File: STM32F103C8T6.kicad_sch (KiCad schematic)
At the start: 28 parts, among them J4 Conn_02x03_Odd_Even, J5 Conn_01x05_Male, J6 Conn_01x04_Male, SW1 PTS810, U3 MCU_STM32F103C8Tx, Y1 16MHz

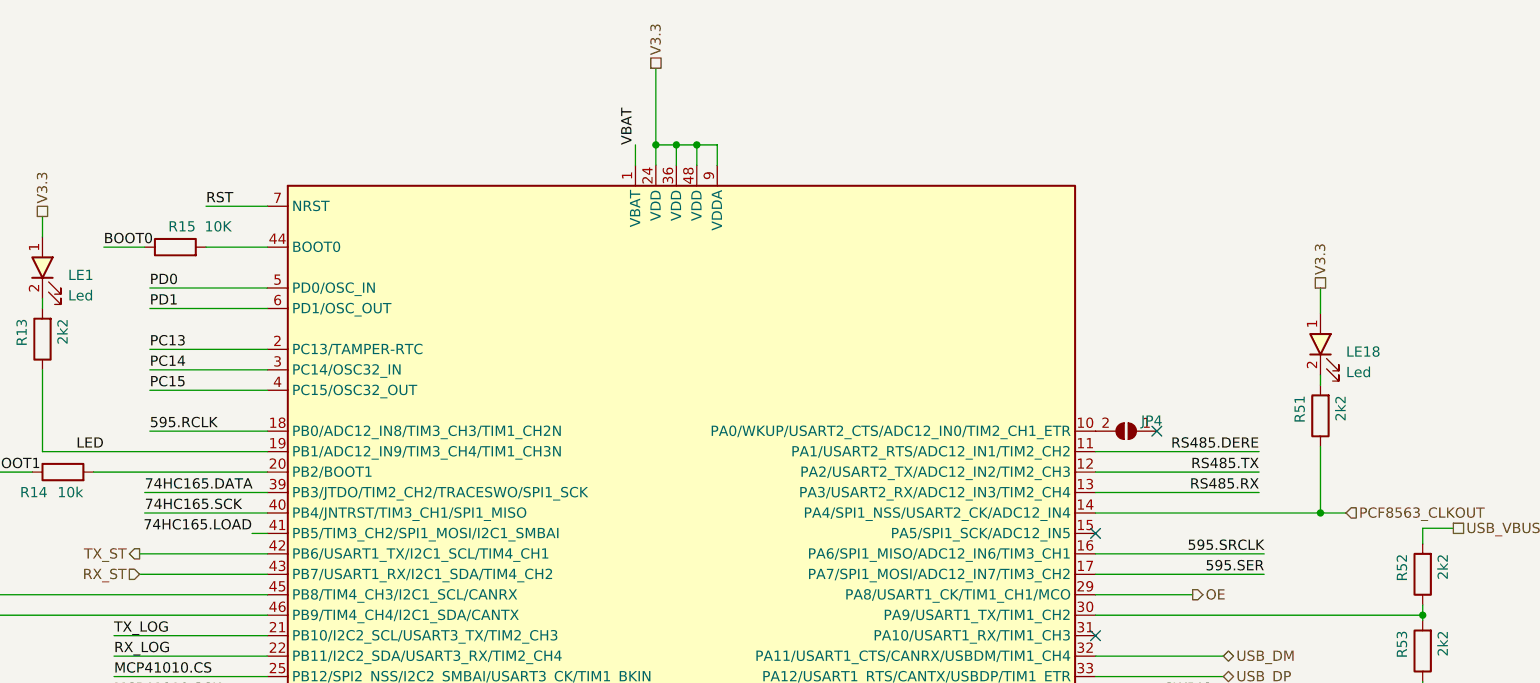
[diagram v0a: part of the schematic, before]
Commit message: finish some unconnect pins, draw edge cut board
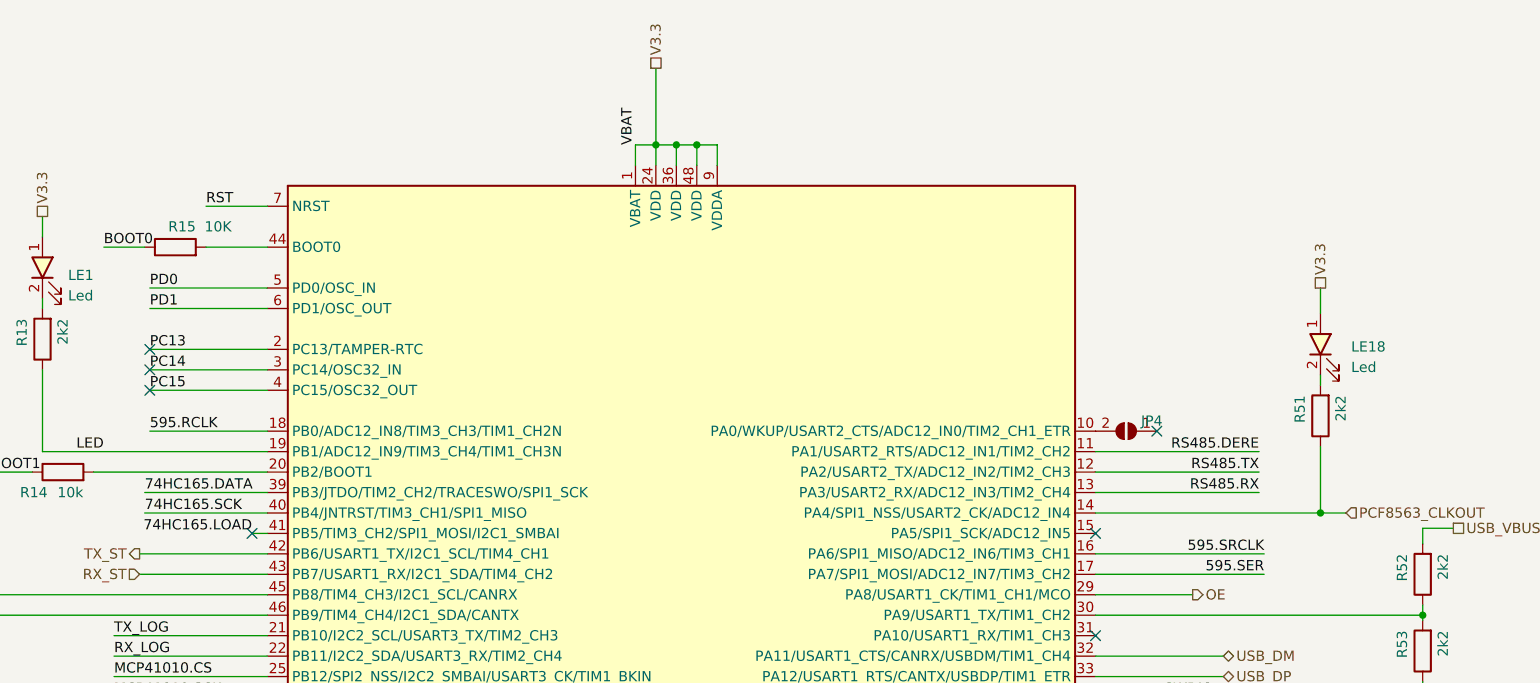
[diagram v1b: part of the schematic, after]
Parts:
- removed LE18: Led, SpiritBoi_Footprint_Library:LED_0603, symbol IVS_SYMBOLS:Led
- added LE18: Led, SpiritBoi_Footprint_Library:LED_0603, symbol SpiritBoi_Library:Led
- JP4: now left out of the parts list
- R14: symbol Thu_vien_kicad:R -> SpiritBoi_Library:R
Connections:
- net VBAT is gone; now on net V3.3: U3.1 (VBAT)
- net V3.3: now also LE18.1
- net at R51.2: now also LE18.2
- no-connect marks 5 -> 9
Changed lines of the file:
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@@
 	)
 	(no_connect
+		(at 156.845 147.32)
+	)
+	(no_connect
+		(at 169.545 170.18)
+	)
+	(no_connect
+		(at 156.845 152.4)
+	)
+	(no_connect
 		(at 274.32 182.88)
 	)
@@
 	)
 	(no_connect
+		(at 156.845 149.86)
+	)
+	(no_connect
 		(at 274.32 170.18)
 	)
@@
 	(wire
 		(pts
+			(xy 217.17 121.92) (xy 219.71 121.92)
+		)
+		(stroke
+			(width 0)
+			(type default)
+		)
+	)
+	(wire
+		(pts
 			(xy 111.76 52.705) (xy 111.76 60.96)
 		)
@@
 		(unit 1)
 		(exclude_from_sim no)
-		(in_bom yes)
+		(in_bom no)
 		(on_board yes)
 		(dnp no)
@@
 	)
 	(symbol
+		(lib_id "SpiritBoi_Library:Led")
+		(at 302.26 147.955 90)
+		(unit 1)
+		(exclude_from_sim no)
+		(in_bom yes)
+		(on_board yes)
+		(dnp no)
+		(fields_autoplaced yes)
+		(property "Reference" "LE18"
+			(at 306.07 147.0024 90)
+			(effects
+				(font
+					(size 1.27 1.27)
+				)
+				(justify right)
+			)
+		)
+		(property "Value" "Led"
+			(at 306.07 149.5424 90)
+			(effects
+				(font
+					(size 1.27 1.27)
+				)
+				(justify right)
+			)
+		)
+		(property "Footprint" "SpiritBoi_Footprint_Library:LED_0603"
+			(at 302.514 147.193 0)
+			(effects
+				(font
+					(size 1.27 1.27)
+				)
+				(hide yes)
+			)
+		)
+		(property "Datasheet" ""
+			(at 302.514 147.193 0)
+			(effects
+				(font
+					(size 1.27 1.27)
+				)
+				(hide yes)
+			)
+		)
+		(property "Description" ""
+			(at 302.26 147.955 0)
+			(effects
+				(font
+					(size 1.27 1.27)
+				)
+				(hide yes)
+			)
+		)
+		(pin "2"
+		)
+		(pin "1"
+		)
+		(instances
+			(project "DongTamV2"
+				(path "/2303d546-b88a-4ab0-aee1-26e3b32ac9d7/de1d919d-cc07-489f-afed-971dd930ed54"
+					(reference "LE18")
+					(unit 1)
+				)
+			)
+		)
+	)
+	(symbol
 		(lib_id "SpiritBoi_Library:MCU_STM32F103C8Tx")
 		(at 222.25 165.1 0)
@@
 			)
 		)
-		(property "Description" ""
+		(property "Description" "Resistor"
 			(at 106.68 170.18 0)
 			(effects
@@
 	)
 	(symbol
-		(lib_id "Thu_vien_kicad:R")
+		(lib_id "SpiritBoi_Library:R")
 		(at 146.05 162.56 90)
 		(unit 1)
@@
 			)
 		)
-		(property "Description" ""
+		(property "Description" "Resistor"
 			(at 146.05 162.56 0)
 			(effects
@@
 					(unit 1)
 				)
-			)
-		)
-	)
-	(symbol
-		(lib_id "IVS_SYMBOLS:Led")
-		(at 302.26 147.955 90)
-		(unit 1)
-		(exclude_from_sim no)
-		(in_bom yes)
-		(on_board yes)
-		(dnp no)
-		(fields_autoplaced yes)
-		(property "Reference" "LE18"
-			(at 305.435 147.6375 90)
-			(effects
-				(font
-					(size 1.27 1.27)
-				)
-				(justify right)
-			)
-		)
-		(property "Value" "Led"
-			(at 305.435 150.1775 90)
-			(effects
-				(font
-					(size 1.27 1.27)
-				)
-				(justify right)
-			)
-		)
-		(property "Footprint" "SpiritBoi_Footprint_Library:LED_0603"
-			(at 302.514 147.193 0)
-			(effects
-				(font
-					(size 1.27 1.27)
-				)
-				(hide yes)
-			)
-		)
-		(property "Datasheet" ""
-			(at 302.514 147.193 0)
-			(effects
-				(font
-					(size 1.27 1.27)
-				)
-				(hide yes)
-			)
-		)
-		(property "Description" ""
-			(at 302.26 147.955 0)
-			(effects
-				(font
-					(size 1.27 1.27)
-				)
-				(hide yes)
-			)
-		)
-		(pin "1"
-		)
-		(pin "2"
-		)
-		(instances
-			(project "DongTamV2"
-				(path "/2303d546-b88a-4ab0-aee1-26e3b32ac9d7/de1d919d-cc07-489f-afed-971dd930ed54"
-					(reference "LE18")
-					(unit 1)
-				)

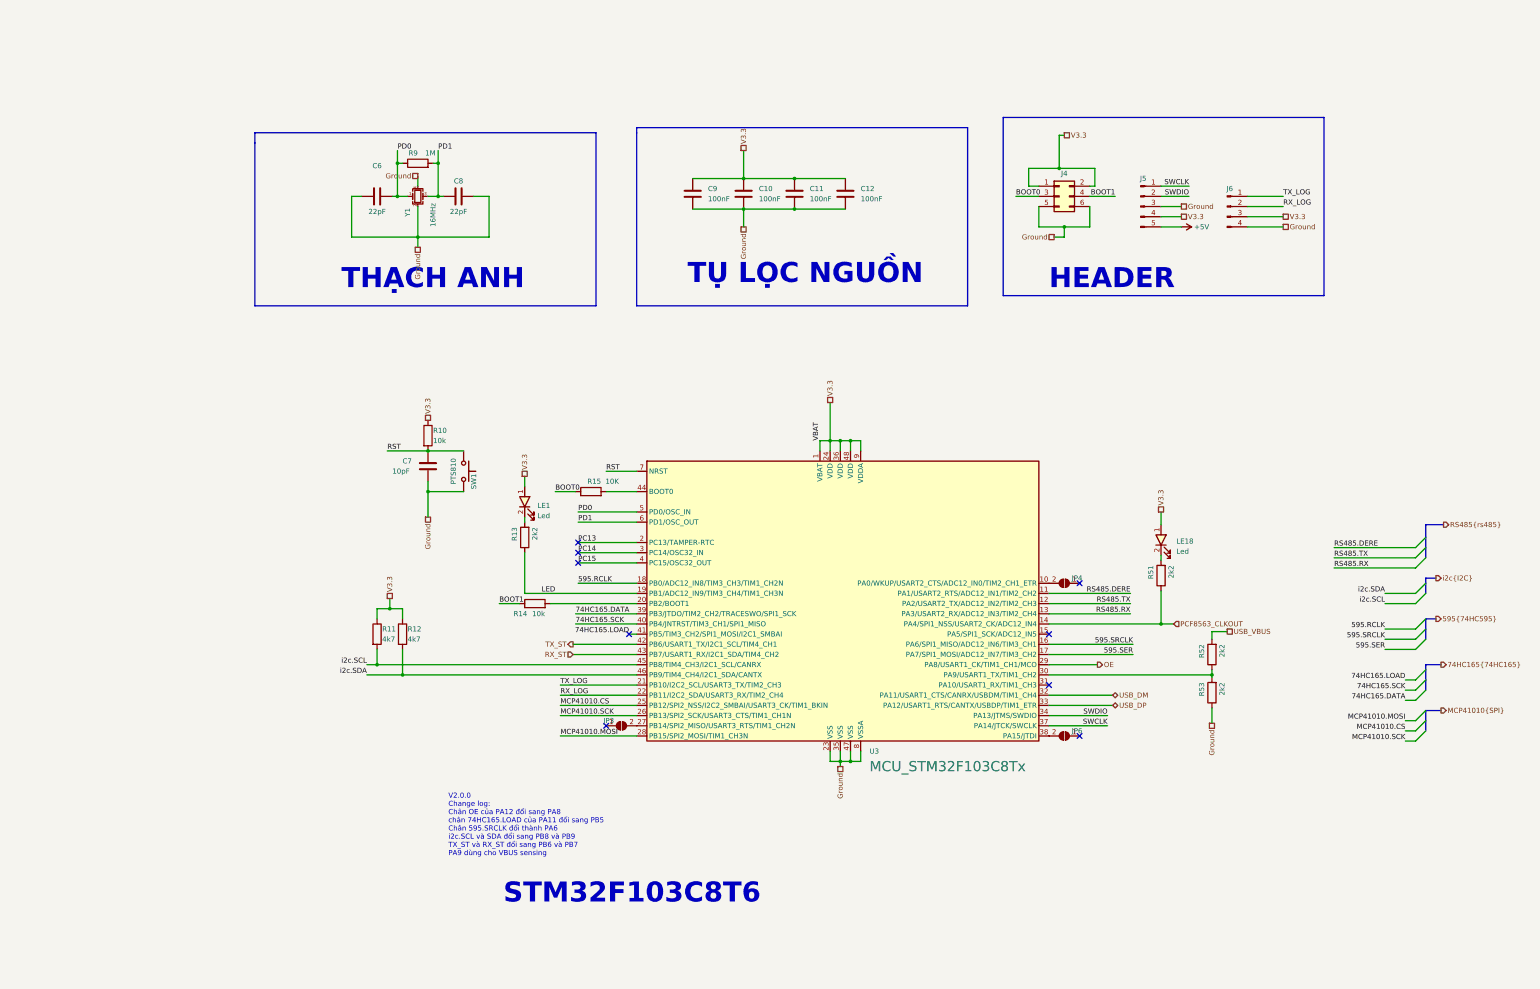
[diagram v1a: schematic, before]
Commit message: Add LORA, SDcard and Volt to 4_20mA scheamtic
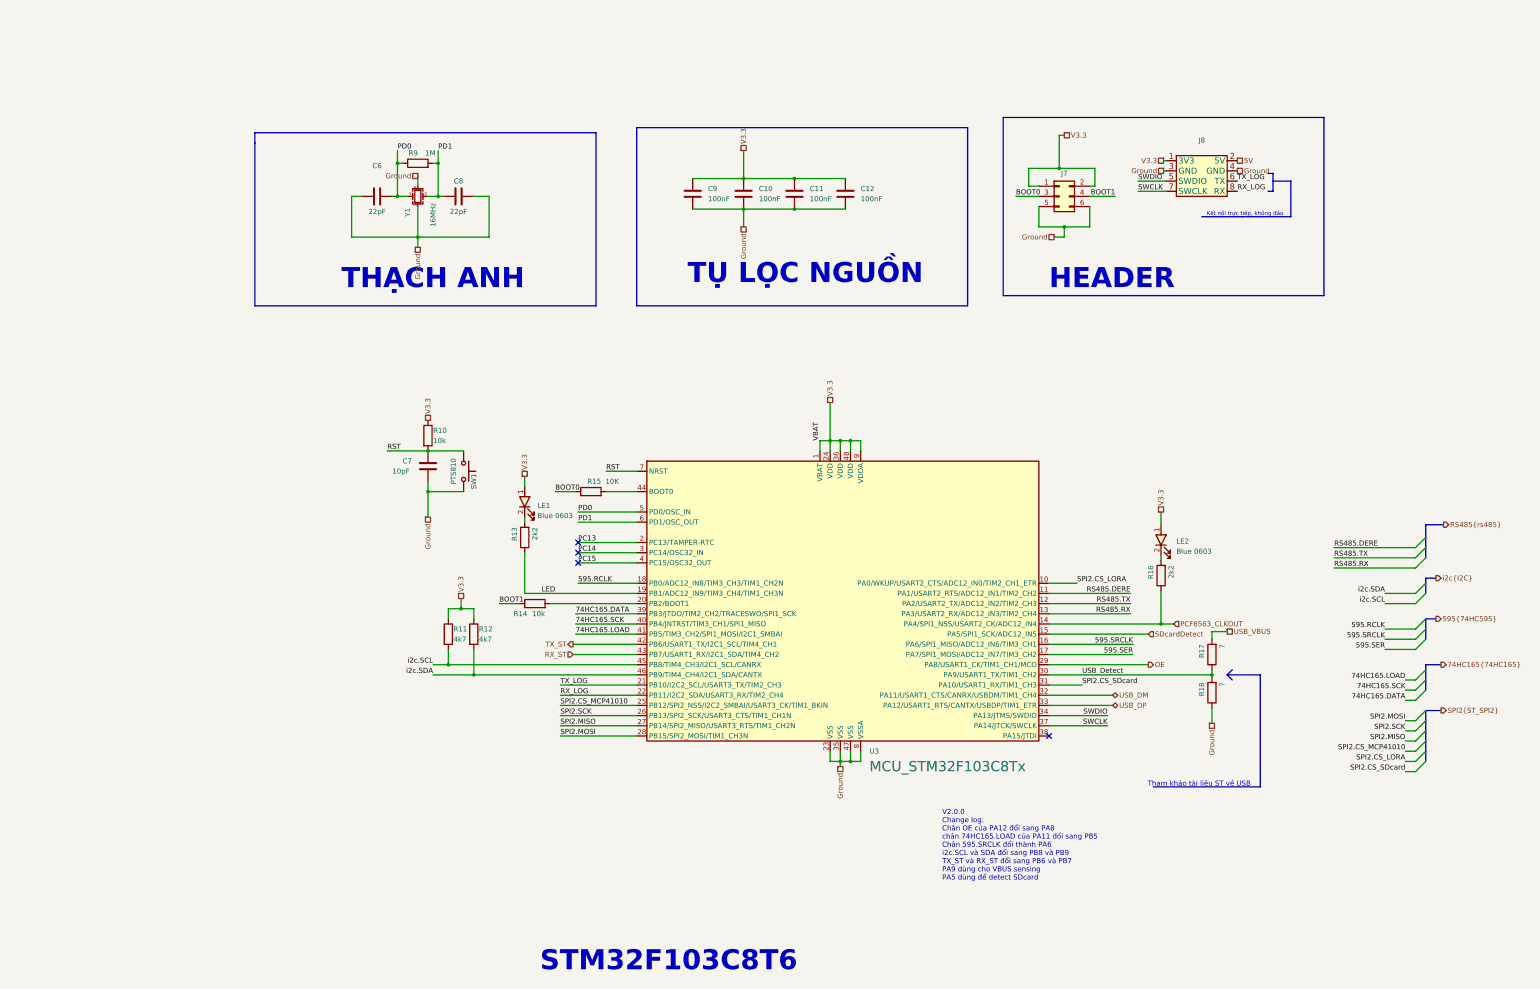
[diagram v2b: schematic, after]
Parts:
- removed J5: Conn_01x05_Male, Connector_PinHeader_2.54mm:PinHeader_1x05_P2.54mm_Vertical, symbol Connector:Conn_01x05_Male
- removed J6: Conn_01x04_Male, Connector_PinHeader_2.54mm:PinHeader_1x04_P2.54mm_Vertical, symbol Connector:Conn_01x04_Male
- removed JP3, JP4, JP6: SolderJumper_2_Open, Jumper:SolderJumper-2_P1.3mm_Open_RoundedPad1.0x1.5mm, symbol Jumper:SolderJumper_2_Open
- added J8: ~, SpiritBoi_Footprint_Library:Conn-Vert-THT-2.54mm-2x4P-IDC_Header, symbol SpiritBoi_Library:STlinkV2.1CustomHeader
- LE1: value Led -> Blue 0603
- LE2: renamed from LE18; value Led -> Blue 0603
- R17: renamed from R52; value 2k2 -> ?
- R18: renamed from R53; value 2k2 -> ?
- renumbered J4 to J7, R51 to R16
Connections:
- net Ground: now also J8.3 (GND), J8.4 (GND)
- net RX_LOG: now also J8.8 (RX)
- net SWCLK: now also J8.7 (SWCLK)
- net SWDIO: now also J8.5 (SWDIO)
- net TX_LOG: now also J8.6 (TX)
- net V3.3: now also J8.1 (3V3)
- net SPI2.CS_LORA: now reaches U3.10 (PA0/WKUP/USART2_CTS/ADC12_IN0/TIM2_CH1_ETR)
- net SDcardDetect: now reaches U3.15 (PA5/SPI1_SCK/ADC12_IN5)
- net SPI2.MISO: now reaches U3.27 (PB14/SPI2_MISO/USART3_RTS/TIM1_CH2N)
- net USB_Detect: now reaches R17.1, R18.2, U3.30 (PA9/USART1_TX/TIM1_CH2)
- net SPI2.CS_SDcard: now reaches U3.31 (PA10/USART1_RX/TIM1_CH3)
- net MCP41010.CS renamed SPI2.CS_MCP41010
- net MCP41010.MOSI renamed SPI2.MOSI
- net MCP41010.SCK renamed SPI2.SCK
- new net 5V: J8.2 (5V)
- no-connect marks 9 -> 4
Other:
- note added: "Kết nối trực tiếp, không đảo"
- note added: "Tham khảo tài liệu ST về USB"
- note added: "V2.0.0 Change log: Chân OE của PA12 đổi sang PA8 chân 74HC165.LOAD của PA11 đổi sang PB5 Chân 595.SRCLK đổi thành PA6 i2c.SCL và SDA đổi sang PB8 và PB9 TX_ST và RX_ST đổi sang PB6 và PB7 PA9 dùng cho VBUS sensing PA5 dùng để detect SDcard"
- note removed: "V2.0.0 Change log: Chân OE của PA12 đổi sang PA8 chân 74HC165.LOAD của PA11 đổi sang PB5 Chân 595.SRCLK đổi thành PA6 i2c.SCL và SDA đổi sang PB8 và PB9 TX_ST và RX_ST đổi sang PB6 và PB7 PA9 dùng cho VBUS sensing"
- moved on the sheet: R11, R12

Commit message: Add README, Lora received interrupt pin
Change LED pin from PB0 to PC13, PCF8563_CLKOUT to PC14
PB0 add Lora received interrupt pin
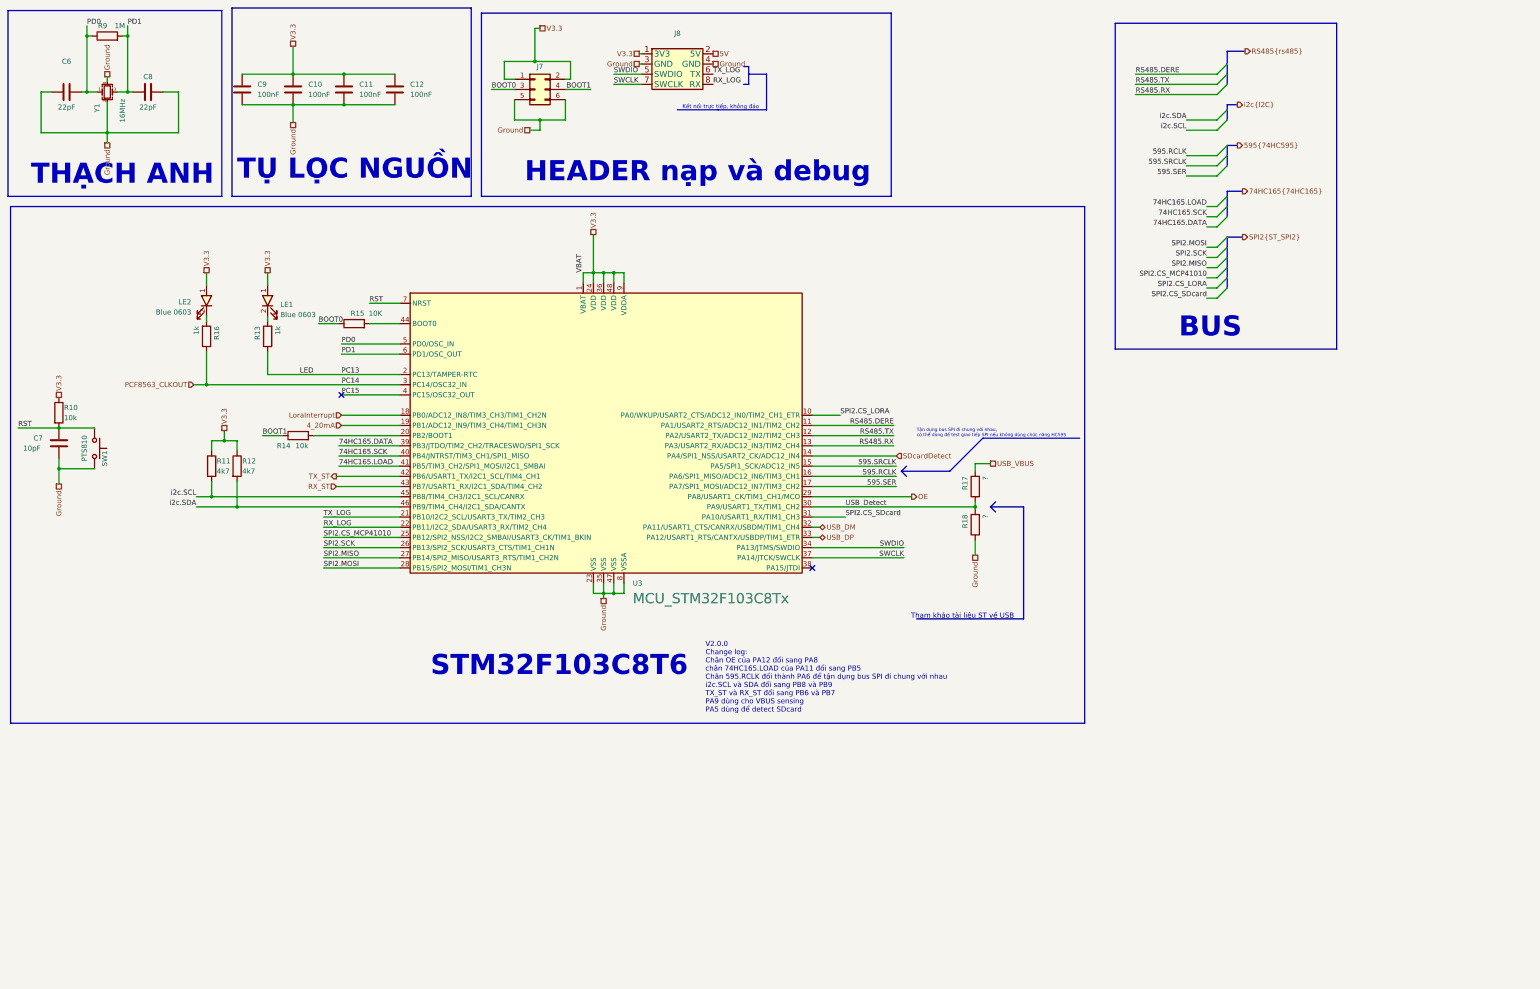
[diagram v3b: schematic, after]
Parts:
- R13, R16: value 2k2 -> 1k
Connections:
- net PC13 is gone; now on net LED: U3.2 (PC13/TAMPER-RTC)
- net PC14 is gone; now on net PCF8563_CLKOUT: U3.3 (PC14/OSC32_IN)
- net 595.RCLK: now also U3.16 (PA6/SPI1_MISO/ADC12_IN6/TIM3_CH1); no longer U3.18 (PB0/ADC12_IN8/TIM3_CH3/TIM1_CH2N)
- net 595.SRCLK: now also U3.15 (PA5/SPI1_SCK/ADC12_IN5); no longer U3.16 (PA6/SPI1_MISO/ADC12_IN6/TIM3_CH1)
- net LED: no longer U3.19 (PB1/ADC12_IN9/TIM3_CH4/TIM1_CH3N)
- net PCF8563_CLKOUT: no longer U3.14 (PA4/SPI1_NSS/USART2_CK/ADC12_IN4)
- net SDcardDetect: now also U3.14 (PA4/SPI1_NSS/USART2_CK/ADC12_IN4); no longer U3.15 (PA5/SPI1_SCK/ADC12_IN5)
- new net 4_20mA: U3.19 (PB1/ADC12_IN9/TIM3_CH4/TIM1_CH3N)
- new net LoraInterrupt: U3.18 (PB0/ADC12_IN8/TIM3_CH3/TIM1_CH2N)
- no-connect marks 4 -> 2
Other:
- note added: "BUS"
- note added: "HEADER nạp và debug"
- note added: "Tận dụng bus SPI đi chung với nhau, có thể dùng để test giao tiếp SPI nếu không dùng chức năng HC595"
- note added: "V2.0.0 Change log: Chân OE của PA12 đổi sang PA8 chân 74HC165.LOAD của PA11 đổi sang PB5 Chân 595.RCLK đổi thành PA6 để tận dụng bus SPI đi chung với nhau i2c.SCL và SDA đổi sang PB8 và PB9 TX_ST và RX_ST đổi sang PB6 và PB7 PA9 dùng cho VBUS sensing PA5 dùng để detect SDcard"
- note removed: "HEADER"
- note removed: "V2.0.0 Change log: Chân OE của PA12 đổi sang PA8 chân 74HC165.LOAD của PA11 đổi sang PB5 Chân 595.SRCLK đổi thành PA6 i2c.SCL và SDA đổi sang PB8 và PB9 TX_ST và RX_ST đổi sang PB6 và PB7 PA9 dùng cho VBUS sensing PA5 dùng để detect SDcard"
- moved on the sheet: C10, C11, C12, C6, C7, C8, C9, J7, J8, LE1, R10, R11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

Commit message: layout p1
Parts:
- removed J7: Conn_02x03_Odd_Even, Connector_PinHeader_2.54mm:PinHeader_2x03_P2.54mm_Vertical, symbol Connector_Generic:Conn_02x03_Odd_Even
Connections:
- net BOOT1 is gone; now on net Ground: R14.1
- net BOOT0: now also R15.2, U3.44 (BOOT0); no longer R15.1
- net Ground: now also R15.1
